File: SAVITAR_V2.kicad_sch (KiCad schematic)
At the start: 0 parts

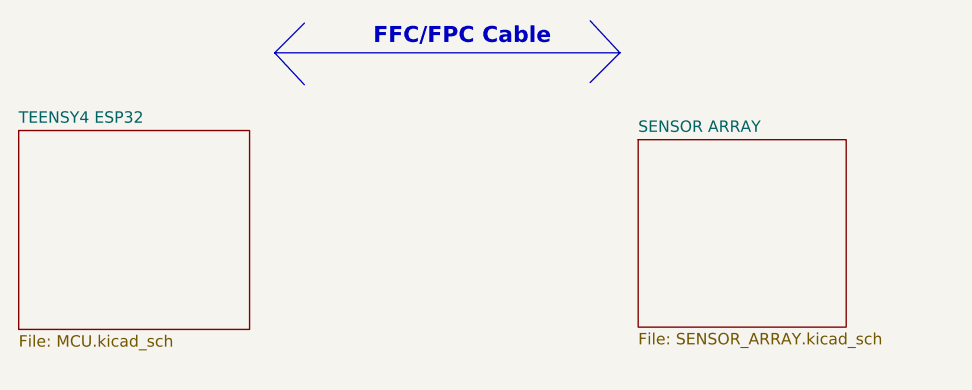
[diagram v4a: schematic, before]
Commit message: Added decoupling for sensor board. Changed the relatively old CD4051BM with over 400 ohm to 74HC4051. Added for the first time hierarchical label to connect the FFC pins across schematics.
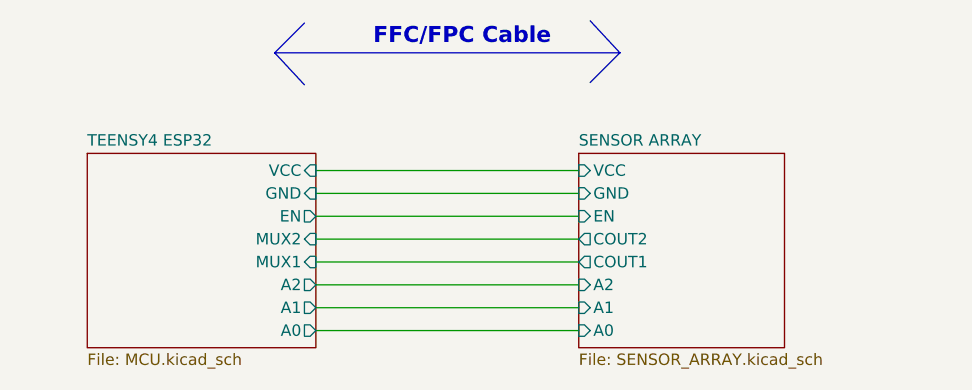
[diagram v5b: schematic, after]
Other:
- sheet SENSOR ARRAY ports: added A0, A1, A2, COUT1, COUT2, EN, GND, VCC; removed none
- sheet TEENSY4 ESP32 ports: added A0, A1, A2, EN, GND, MUX1, MUX2, VCC; removed none
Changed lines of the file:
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@@
+		)
+	)
+	(wire
+		(pts
+			(xy 52.07 52.705) (xy 81.28 52.705)
+		)
+		(stroke
+			(width 0)
+			(type default)
 		)
 	)
@@
 		)
 	)
+	(wire
+		(pts
+			(xy 52.07 42.545) (xy 81.28 42.545)
+		)
+		(stroke
+			(width 0)
+			(type default)
+		)
+	)
+	(wire
+		(pts
+			(xy 52.07 45.085) (xy 81.28 45.085)
+		)
+		(stroke
+			(width 0)
+			(type default)
+		)
+	)
 	(polyline
 		(pts
@@
 		)
 	)
+	(wire
+		(pts
+			(xy 52.07 55.245) (xy 81.28 55.245)
+		)
+		(stroke
+			(width 0)
+			(type default)
+		)
+	)
 	(polyline
 		(pts
@@
 		)
 	)
+	(wire
+		(pts
+			(xy 52.07 40.005) (xy 81.28 40.005)
+		)
+		(stroke
+			(width 0)
+			(type default)
+		)
+	)
+	(wire
+		(pts
+			(xy 52.07 47.625) (xy 81.28 47.625)
+		)
+		(stroke
+			(width 0)
+			(type default)
+		)
+	)
+	(wire
+		(pts
+			(xy 52.07 57.785) (xy 81.28 57.785)
+		)
+		(stroke
+			(width 0)
+			(type default)
+		)
+	)
 	(polyline
 		(pts
@@
 		)
 	)
+	(wire
+		(pts
+			(xy 52.07 50.165) (xy 81.28 50.165)
+		)
+		(stroke
+			(width 0)
+			(type default)
+		)
+	)
 	(polyline
 		(pts
@@
 	)
 	(sheet
-		(at 19.05 35.56)
-		(size 25.654 22.098)
+		(at 26.67 38.1)
+		(size 25.4 21.59)
 		(exclude_from_sim no)
 		(in_bom yes)
@@
 		)
 		(property "Sheetname" "TEENSY4 ESP32"
-			(at 19.05 34.8484 0)
+			(at 26.67 37.3884 0)
 			(show_name no)
 			(do_not_autoplace no)
@@
 		)
 		(property "Sheetfile" "MCU.kicad_sch"
-			(at 19.05 58.2426 0)
+			(at 26.67 60.2746 0)
 			(show_name no)
 			(do_not_autoplace no)
@@
 				)
 				(justify left top)
+			)
+		)
+		(pin "A0" output
+			(at 52.07 57.785 0)
+			(effects
+				(font
+					(size 1.27 1.27)
+				)
+				(justify right)
+			)
+		)
+		(pin "A1" output
+			(at 52.07 55.245 0)
+			(effects
+				(font
+					(size 1.27 1.27)
+				)
+				(justify right)
+			)
+		)
+		(pin "A2" output
+			(at 52.07 52.705 0)
+			(effects
+				(font
+					(size 1.27 1.27)
+				)
+				(justify right)
+			)
+		)
+		(pin "EN" output
+			(at 52.07 45.085 0)
+			(effects
+				(font
+					(size 1.27 1.27)
+				)
+				(justify right)
+			)
+		)
+		(pin "MUX1" input
+			(at 52.07 50.165 0)
+			(effects
+				(font
+					(size 1.27 1.27)
+				)
+				(justify right)
+			)
+		)
+		(pin "MUX2" input
+			(at 52.07 47.625 0)
+			(effects
+				(font
+					(size 1.27 1.27)
+				)
+				(justify right)
+			)
+		)
+		(pin "GND" input
+			(at 52.07 42.545 0)
+			(effects
+				(font
+					(size 1.27 1.27)
+				)
+				(justify right)
+			)
+		)
+		(pin "VCC" input
+			(at 52.07 40.005 0)
+			(effects
+				(font
+					(size 1.27 1.27)
+				)
+				(justify right)
 			)
 		)
@@
 	)
 	(sheet
-		(at 87.884 36.576)
-		(size 23.114 20.828)
+		(at 81.28 38.1)
+		(size 22.86 21.59)
 		(exclude_from_sim no)
 		(in_bom yes)
@@
 		)
 		(property "Sheetname" "SENSOR ARRAY"
-			(at 87.884 35.8644 0)
+			(at 81.28 37.3884 0)
 			(show_name no)
 			(do_not_autoplace no)
@@
 		)
 		(property "Sheetfile" "SENSOR_ARRAY.kicad_sch"
-			(at 87.884 57.9886 0)
+			(at 81.28 60.2746 0)
 			(show_name no)
 			(do_not_autoplace no)
@@
 			)
 		)
+		(pin "A0" input
+			(at 81.28 57.785 180)
+			(effects
+				(font
+					(size 1.27 1.27)
+				)
+				(justify left)
+			)
+		)
+		(pin "A1" input
+			(at 81.28 55.245 180)
+			(effects
+				(font
+					(size 1.27 1.27)
+				)
+				(justify left)
+			)
+		)
+		(pin "A2" input
+			(at 81.28 52.705 180)
+			(effects
+				(font
+					(size 1.27 1.27)
+				)
+				(justify left)
+			)
+		)
+		(pin "COUT1" output
+			(at 81.28 50.165 180)
+			(effects
+				(font
+					(size 1.27 1.27)
+				)
+				(justify left)
+			)
+		)
+		(pin "COUT2" output
+			(at 81.28 47.625 180)
+			(effects
+				(font
+					(size 1.27 1.27)
+				)
+				(justify left)
+			)
+		)
+		(pin "EN" input
+			(at 81.28 45.085 180)
+			(effects
+				(font
+					(size 1.27 1.27)
+				)
+				(justify left)
+			)
+		)
+		(pin "GND" input
+			(at 81.28 42.545 180)
+			(effects
+				(font
+					(size 1.27 1.27)
+				)
+				(justify left)
+			)
+		)
+		(pin "VCC" input
+			(at 81.28 40.005 180)
+			(effects
+				(font
+					(size 1.27 1.27)
+				)
+				(justify left)
+			)
+		)

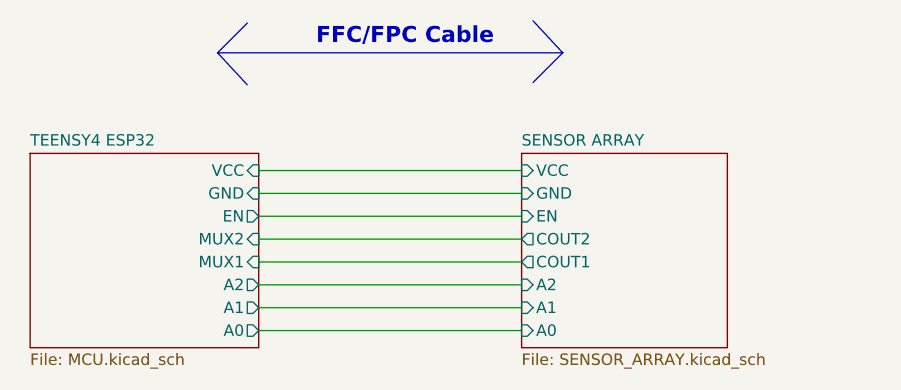
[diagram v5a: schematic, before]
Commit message: Added 3D models to third party footprints. Final Teensy version, switching to SAMD51 custom setup. Please add tag.
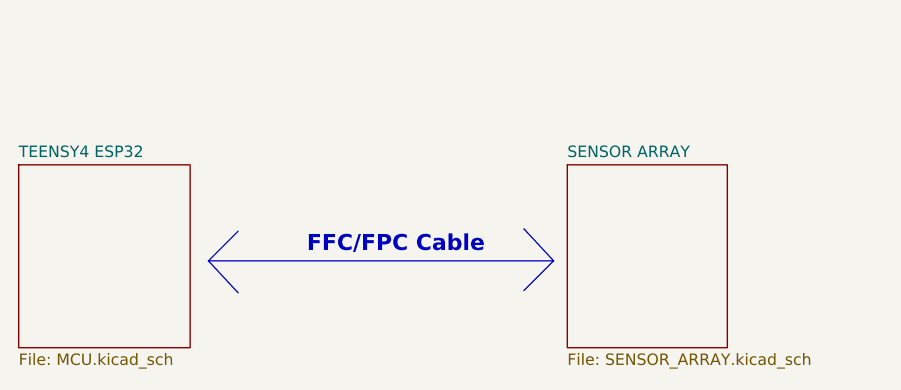
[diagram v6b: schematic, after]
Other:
- sheet SENSOR ARRAY ports: added none; removed A0, A1, A2, COUT1, COUT2, EN, GND, VCC
- sheet TEENSY4 ESP32 ports: added none; removed A0, A1, A2, EN, GND, MUX1, MUX2, VCC

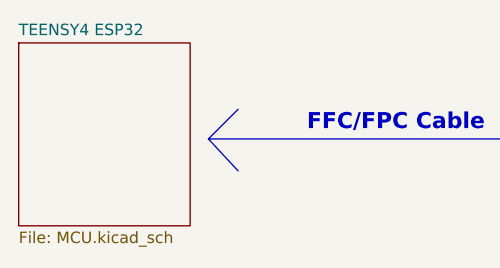
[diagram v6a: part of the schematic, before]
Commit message: Made passives smaller from 0603 to 0402 because I will solder them with hot air gun anyway. Started positioning SAMD51 bypass caps.
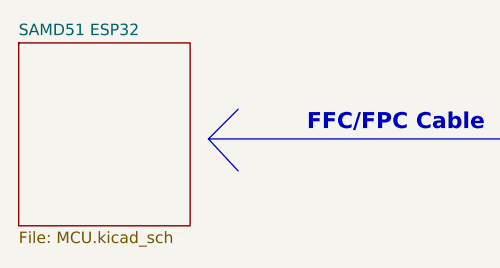
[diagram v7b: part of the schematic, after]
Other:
- sheet TEENSY4 ESP32 renamed SAMD51 ESP32
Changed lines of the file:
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@@
 			(color 0 0 0 0)
 		)
-		(property "Sheetname" "TEENSY4 ESP32"
+		(property "Sheetname" "SAMD51 ESP32"
 			(at 25.4 38.6584 0)
 			(show_name no)
